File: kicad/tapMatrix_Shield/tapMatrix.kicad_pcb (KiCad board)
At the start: 2 copper layers, 68.6 x 53.3 mm, 29 parts, among them IC1 DS1307, P5 TS_ZIF, P6 LED_MATRIX_HDR, U1 APE8865N-33-HF-3, U2 MCP4921-E/SN, U3 74LS125, U4 TL072, U5 SD_CARD

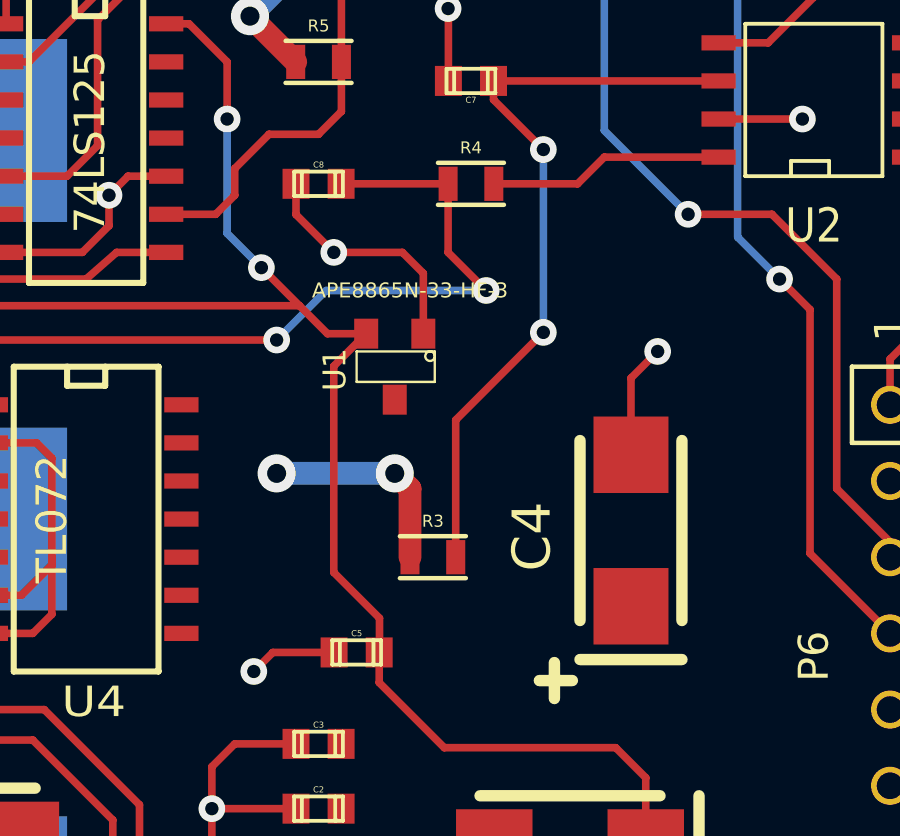
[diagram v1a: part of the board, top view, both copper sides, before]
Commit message: replace voltage regulator with corrected component
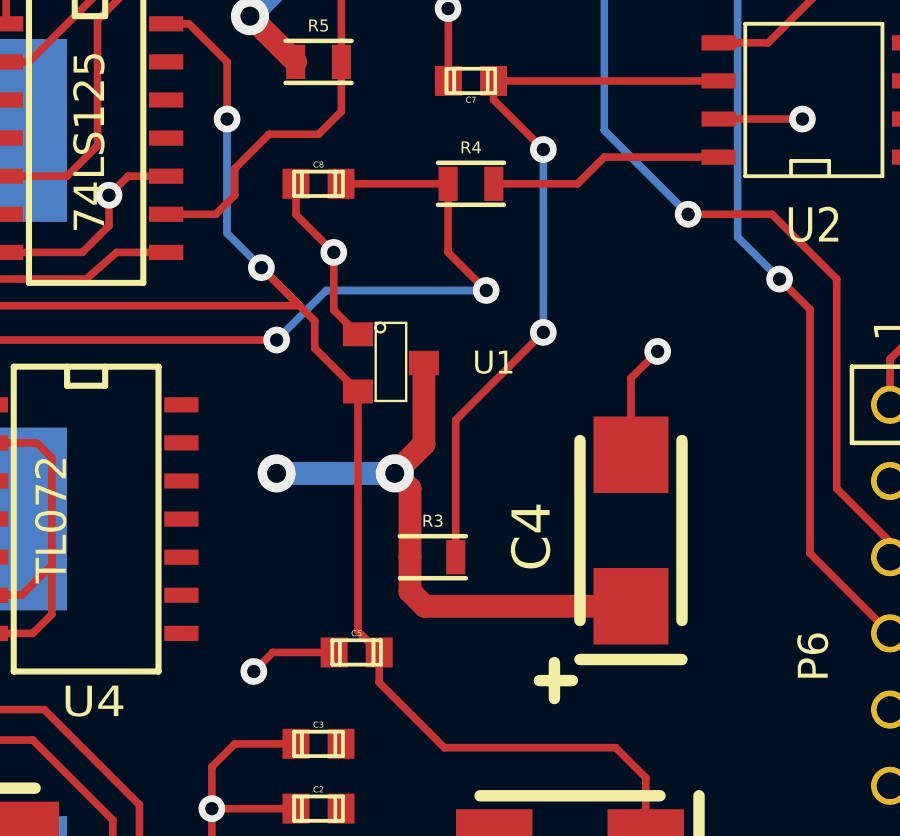
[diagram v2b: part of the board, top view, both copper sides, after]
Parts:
- U1: value APE8865N-33-HF-3 -> MCP1700T-3302E/MB
- moved U1 0.18 mm to (167.5, 106.6), turned to 270 degrees
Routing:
- net +5V: track 32.6 -> 45.4 mm
- net GND: track 94.1 -> 91.9 mm
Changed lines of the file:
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@@
     (thickness 1.6)
     (drawings 98)
-    (tracks 340)
+    (tracks 343)
     (zones 0)
     (modules 29)
@@
   (title_block
     (title "tapMatrix Shield: Footprint")
-    (date "24 Aug 2014")
-    (rev 0.1)
+    (date "03 Sep 2014")
+    (rev 0.2)
     (company "Responsive Devices Inc")
   )
@@
     )
   )
-  (module SMD_Packages:SOT-23 placed (layer F.Cu)
-    (at 167.64 106.68 180)
-    (tags SOT23)
-    (fp_text reference U1 (at 1.99898 -0.09906 270) (layer F.SilkS)
-      (effects (font (size 0.762 0.762) (thickness 0.11938)))
-    )
-    (fp_text value APE8865N-33-HF-3 (at -0.508 2.54 180) (layer F.SilkS)
-      (effects (font (size 0.50038 0.50038) (thickness 0.09906)))
-    )
-    (fp_circle (center -1.17602 0.35052) (end -1.30048 0.44958) (layer F.SilkS) (width 0.07874))
-    (fp_line (start 1.27 -0.508) (end 1.27 0.508) (layer F.SilkS) (width 0.07874))
-    (fp_line (start -1.3335 -0.508) (end -1.3335 0.508) (layer F.SilkS) (width 0.07874))
-    (fp_line (start 1.27 0.508) (end -1.3335 0.508) (layer F.SilkS) (width 0.07874))
-    (fp_line (start -1.3335 -0.508) (end 1.27 -0.508) (layer F.SilkS) (width 0.07874))
-    (pad 3 smd rect (at 0 -1.09982 180) (size 0.8001 1.00076) (layers F.Cu F.Paste F.Mask)
-      (net 1 +5V))
-    (pad 2 smd rect (at 0.9525 1.09982 180) (size 0.8001 1.00076) (layers F.Cu F.Paste F.Mask)
-      (net 49 +3.3V))
-    (pad 1 smd rect (at -0.9525 1.09982 180) (size 0.8001 1.00076) (layers F.Cu F.Paste F.Mask)
-      (net 2 GND))
-    (model smd\SOT23_3.wrl
-      (at (xyz 0 0 0))
-      (scale (xyz 0.4000000059604645 0.4000000059604645 0.4000000059604645))
-      (rotate (xyz 0 0 180))
-    )
-  )
   (module SMD_Packages:SOIC-8-N placed (layer F.Cu)
     (at 181.61 97.79 90)
@@
       (scale (xyz 1 1 1))
       (rotate (xyz 0 0 0))
+    )
+  )
+  (module SMD_Packages:SOT-23 (layer F.Cu)
+    (at 167.513 106.553 270)
+    (tags SOT23)
+    (fp_text reference U1 (at 0 -3.429 360) (layer F.SilkS)
+      (effects (font (size 0.762 0.762) (thickness 0.11938)))
+    )
+    (fp_text value MCP1700T-3302E/MB (at -1.905 -2.667 360) (layer F.SilkS) hide
+      (effects (font (size 0.50038 0.50038) (thickness 0.09906)))
+    )
+    (fp_circle (center -1.17602 0.35052) (end -1.30048 0.44958) (layer F.SilkS) (width 0.07874))
+    (fp_line (start 1.27 -0.508) (end 1.27 0.508) (layer F.SilkS) (width 0.07874))
+    (fp_line (start -1.3335 -0.508) (end -1.3335 0.508) (layer F.SilkS) (width 0.07874))
+    (fp_line (start 1.27 0.508) (end -1.3335 0.508) (layer F.SilkS) (width 0.07874))
+    (fp_line (start -1.3335 -0.508) (end 1.27 -0.508) (layer F.SilkS) (width 0.07874))
+    (pad 3 smd rect (at 0 -1.09982 270) (size 0.8001 1.00076) (layers F.Cu F.Paste F.Mask)
+      (net 1 +5V))
+    (pad 2 smd rect (at 0.9525 1.09982 270) (size 0.8001 1.00076) (layers F.Cu F.Paste F.Mask)
+      (net 49 +3.3V))
+    (pad 1 smd rect (at -0.9525 1.09982 270) (size 0.8001 1.00076) (layers F.Cu F.Paste F.Mask)
+      (net 2 GND))
+    (model smd\SOT23_3.wrl
+      (at (xyz 0 0 0))
+      (scale (xyz 0.4000000059604645 0.4000000059604645 0.4000000059604645))
+      (rotate (xyz 0 0 180))
     )
   )
@@
   (gr_line (start 0 0) (end 66.04 0) (layer Dwgs.User) (width 0.1))
   (gr_line (start 0 0) (end 0 -53.34) (layer Dwgs.User) (width 0.1))
+  (segment (start 168.148 113.03) (end 168.148 114.173) (width 0.762) (layer F.Cu) (net 1) (status 400000))
+  (segment (start 168.64076 114.66576) (end 175.514 114.66576) (width 0.762) (layer F.Cu) (net 1) (status 800000))
+  (segment (start 168.148 114.173) (end 168.64076 114.66576) (width 0.762) (layer F.Cu) (net 1))
+  (segment (start 168.61282 106.553) (end 168.61282 109.26318) (width 0.762) (layer F.Cu) (net 1) (status 400000))
+  (segment (start 168.61282 109.26318) (end 167.64 110.236) (width 0.762) (layer F.Cu) (net 1))
   (segment (start 184.785 99.695) (end 187.198 99.695) (width 0.762) (layer F.Cu) (net 1))
   (via (at 193.167 108.712) (size 1.27) (layers F.Cu B.Cu) (net 1))
@@
   (via (at 167.64 110.236) (size 1.27) (layers F.Cu B.Cu) (net 1))
   (segment (start 168.148 110.744) (end 167.64 110.236) (width 0.762) (layer F.Cu) (net 1))
+  (segment (start 165.608 102.87) (end 165.608 104.79532) (width 0.254) (layer F.Cu) (net 2))
+  (segment (start 164.34816 101.61016) (end 165.608 102.87) (width 0.254) (layer F.Cu) (net 2))
+  (via (at 165.608 102.87) (size 0.889) (layers F.Cu B.Cu) (net 2))
+  (segment (start 164.34816 100.584) (end 164.34816 101.61016) (width 0.254) (layer F.Cu) (net 2))
+  (segment (start 165.608 104.79532) (end 166.41318 105.6005) (width 0.254) (layer F.Cu) (net 2) (status 800000))
   (segment (start 178.435 98.425) (end 181.229 98.425) (width 0.254) (layer F.Cu) (net 2))
   (via (at 181.229 98.425) (size 0.889) (layers F.Cu B.Cu) (net 2))
@@
   (segment (start 140.843 88.138) (end 133.731 88.138) (width 0.254) (layer F.Cu) (net 2))
   (segment (start 142.085 89.38) (end 140.843 88.138) (width 0.254) (layer F.Cu) (net 2))
-  (segment (start 168.5925 105.58018) (end 168.5925 103.5685) (width 0.254) (layer F.Cu) (net 2))
-  (segment (start 164.34816 101.61016) (end 164.34816 100.584) (width 0.254) (layer F.Cu) (net 2))
-  (via (at 165.608 102.87) (size 0.889) (layers F.Cu B.Cu) (net 2))
-  (segment (start 164.34816 101.61016) (end 165.608 102.87) (width 0.254) (layer F.Cu) (net 2))
-  (segment (start 167.894 102.87) (end 165.608 102.87) (width 0.254) (layer F.Cu) (net 2))
-  (segment (start 168.5925 103.5685) (end 167.894 102.87) (width 0.254) (layer F.Cu) (net 2))
   (segment (start 169.672 113.03) (end 169.672 108.458) (width 0.254) (layer F.Cu) (net 3))
   (segment (start 170.93184 97.77984) (end 170.93184 97.155) (width 0.254) (layer F.Cu) (net 3))
@@
   (segment (start 144.526 101.6) (end 154.686 101.6) (width 0.254) (layer F.Cu) (net 48))
   (segment (start 139.256 96.33) (end 144.526 101.6) (width 0.254) (layer F.Cu) (net 48))
+  (segment (start 163.195 103.378) (end 164.973 105.156) (width 0.254) (layer F.Cu) (net 49))
+  (segment (start 164.973 106.06532) (end 166.41318 107.5055) (width 0.254) (layer F.Cu) (net 49) (status 800000))
+  (segment (start 164.973 105.156) (end 164.973 106.06532) (width 0.254) (layer F.Cu) (net 49))
+  (segment (start 166.41318 107.5055) (end 166.41318 115.49634) (width 0.254) (layer F.Cu) (net 49) (status 400000))
+  (segment (start 166.41318 115.49634) (end 167.12184 116.205) (width 0.254) (layer F.Cu) (net 49) (status 800000))
   (segment (start 167.12184 116.205) (end 167.12184 117.21084) (width 0.254) (layer F.Cu) (net 49))
   (segment (start 176.00676 120.38076) (end 176.00676 122.682) (width 0.254) (layer F.Cu) (net 49))
@@
   (segment (start 167.12184 117.21084) (end 169.291 119.38) (width 0.254) (layer F.Cu) (net 49))
   (segment (start 167.12184 116.205) (end 167.132 116.19484) (width 0.254) (layer F.Cu) (net 49))
-  (segment (start 167.132 116.19484) (end 167.132 115.062) (width 0.254) (layer F.Cu) (net 49))
-  (segment (start 167.132 115.062) (end 165.608 113.538) (width 0.254) (layer F.Cu) (net 49))
-  (segment (start 165.608 113.538) (end 165.608 106.65968) (width 0.254) (layer F.Cu) (net 49))
-  (segment (start 165.608 106.65968) (end 166.6875 105.58018) (width 0.254) (layer F.Cu) (net 49))
   (segment (start 136.12 95.23) (end 134.894 95.23) (width 0.254) (layer F.Cu) (net 49))
   (segment (start 135.89 104.648) (end 164.465 104.648) (width 0.254) (layer F.Cu) (net 49))
@@
   (segment (start 134.366 95.758) (end 134.366 103.124) (width 0.254) (layer F.Cu) (net 49))
   (segment (start 134.894 95.23) (end 134.366 95.758) (width 0.254) (layer F.Cu) (net 49))
-  (segment (start 166.6875 105.58018) (end 165.39718 105.58018) (width 0.254) (layer F.Cu) (net 49))
   (segment (start 160.782 95.25) (end 160.02 95.25) (width 0.254) (layer F.Cu) (net 49))
   (segment (start 162.052 96.52) (end 160.782 95.25) (width 0.254) (layer F.Cu) (net 49))
@@
   (segment (start 163.195 103.378) (end 162.052 102.235) (width 0.254) (layer B.Cu) (net 49))
   (via (at 163.195 103.378) (size 0.889) (layers F.Cu B.Cu) (net 49))
-  (segment (start 165.39718 105.58018) (end 164.465 104.648) (width 0.254) (layer F.Cu) (net 49))
   (segment (start 164.465 104.648) (end 163.195 103.378) (width 0.254) (layer F.Cu) (net 49))
   (zone (net 1) (net_name +5V) (layer F.Cu) (hatch edge 0.508)

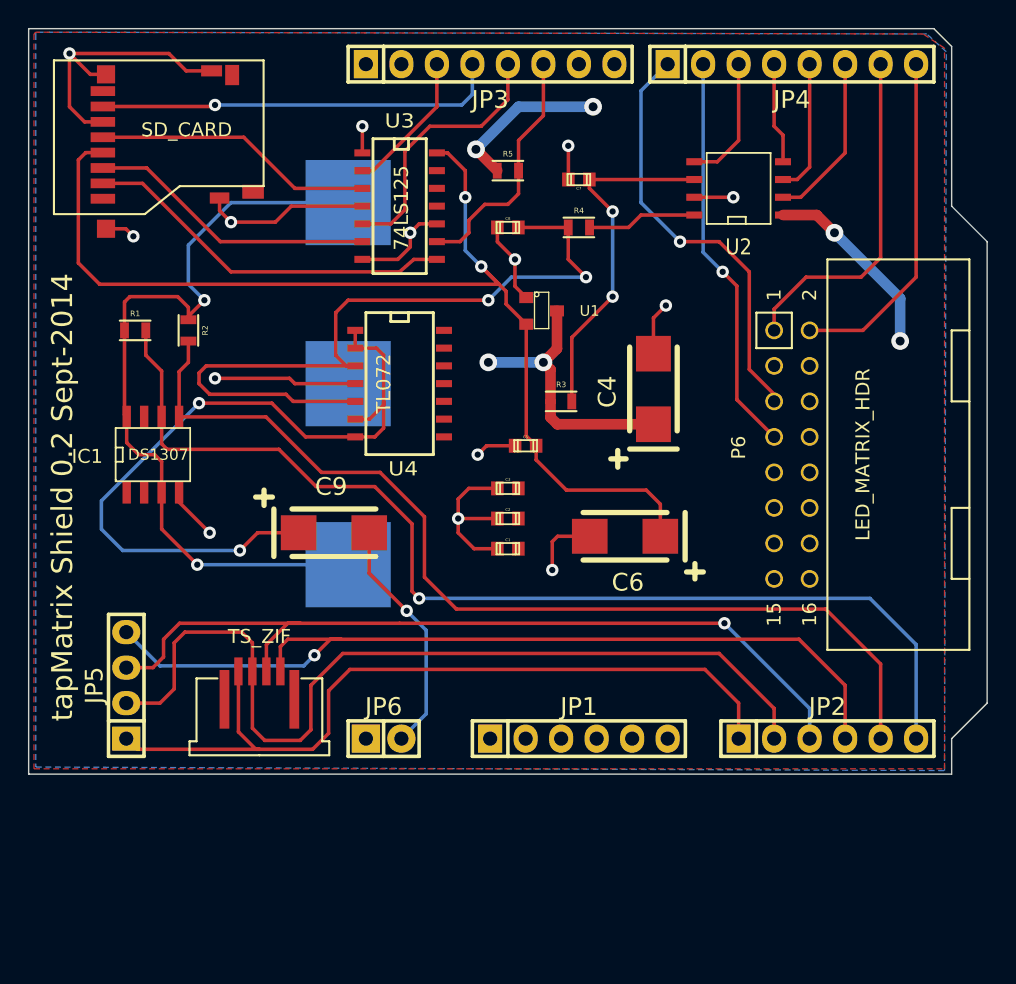
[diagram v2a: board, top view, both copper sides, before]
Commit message: create v0.3_ fix problems with U1, U3, U4 components U1 used the wrong footprint. changed from SOT-23 to SOT-89-3 U3 used the narrow version of SOIC-14 (incorrectly named in library as SOIC-14_W). changed to actual SOIC-14-Wide U4 incorrectly used SOIC-14 footprint. changed to SOIC-8 tore up the layout, placed new footprints. still need to reroute everything
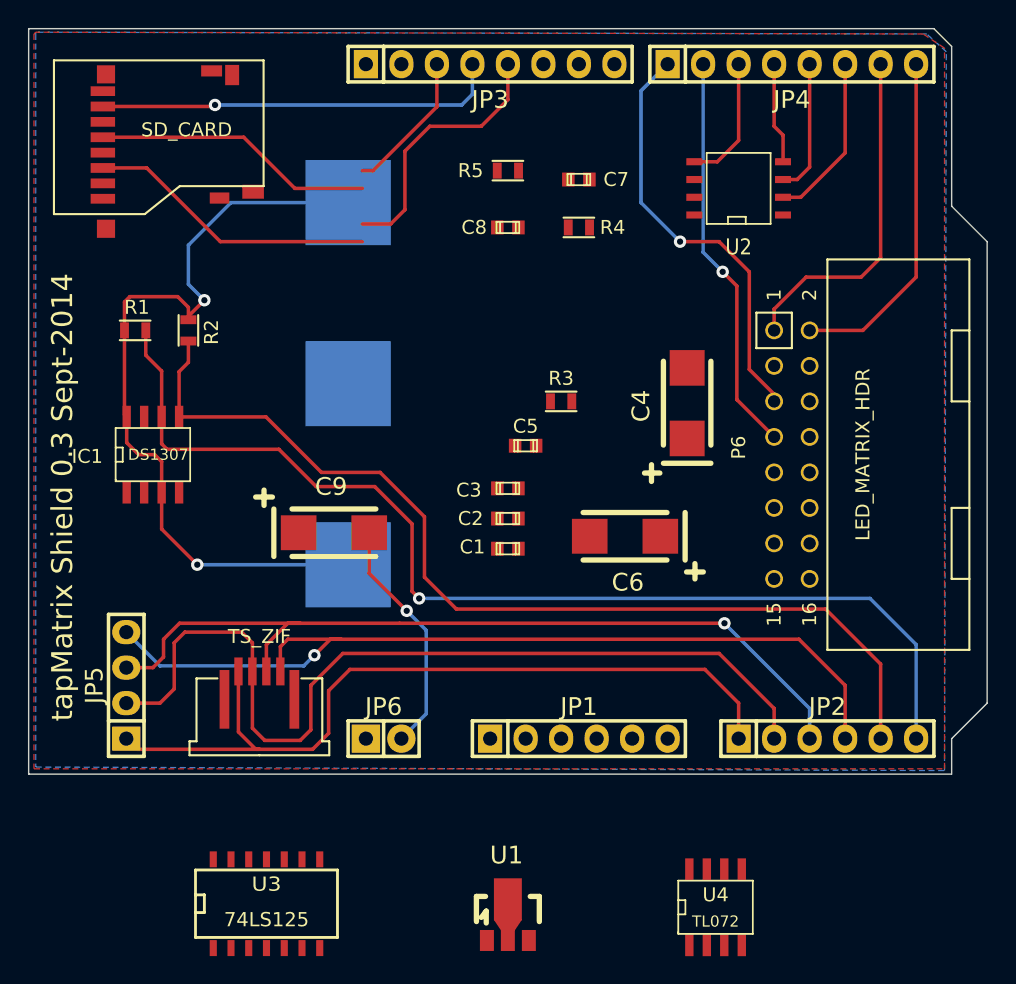
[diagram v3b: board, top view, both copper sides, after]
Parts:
- U1: footprint SMD_Packages:SOT-23 -> Housings_SOT-89:SOT89-3_Housing
- U3: footprint SMD_Packages:SOIC-14_W -> SMD_Packages:SOIC-14_N
- U4: footprint SMD_Packages:SOIC-14_N -> Housings_SOIC:SOIC-8_N
- moved U3 50.7 mm to (147.8, 148.8), turned to 0 degrees
- moved U4 43.7 mm to (180.0, 149.2), turned to 0 degrees
- moved U1 43.3 mm to (165.1, 149.8), turned to 0 degrees
- moved C4 2.62 mm to (177.9, 113.2)
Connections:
- C5 pad 1: +3.3V -> VCC
- C6 pad 1: +3.3V -> VCC
- U1 pad 2: +3.3V -> +5V
- U1 pad 3: +5V -> VCC
- U3 pad 14: +3.3V -> VCC
- U5 pad 4: +3.3V -> VCC
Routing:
- net GND: track 91.9 -> 0.00 mm, vias 14 -> 0
- net +3.3V: track 79.7 -> 0.00 mm, vias 2 -> 0
- net Net-(C8-Pad1): track 55.2 -> 0.00 mm, vias 2 -> 0
- net Net-(C9-Pad1): track 53.1 -> 0.00 mm, vias 2 -> 0
- net +5V: track 45.4 -> 0.00 mm, vias 6 -> 0
- net /CS: track 26.9 -> 0.00 mm
- net Net-(C7-Pad2): track 25.3 -> 0.00 mm, vias 2 -> 0
- net /SD_CS: track 17.8 -> 0.00 mm
- net Net-(R4-Pad2): track 7.86 -> 0.00 mm
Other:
- board text added: "tapMatrix Shield 0.3 Sept-2014"
- board text removed: "tapMatrix Shield 0.2 Sept-2014"

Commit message: Revised r0.3 components, tore up pcb
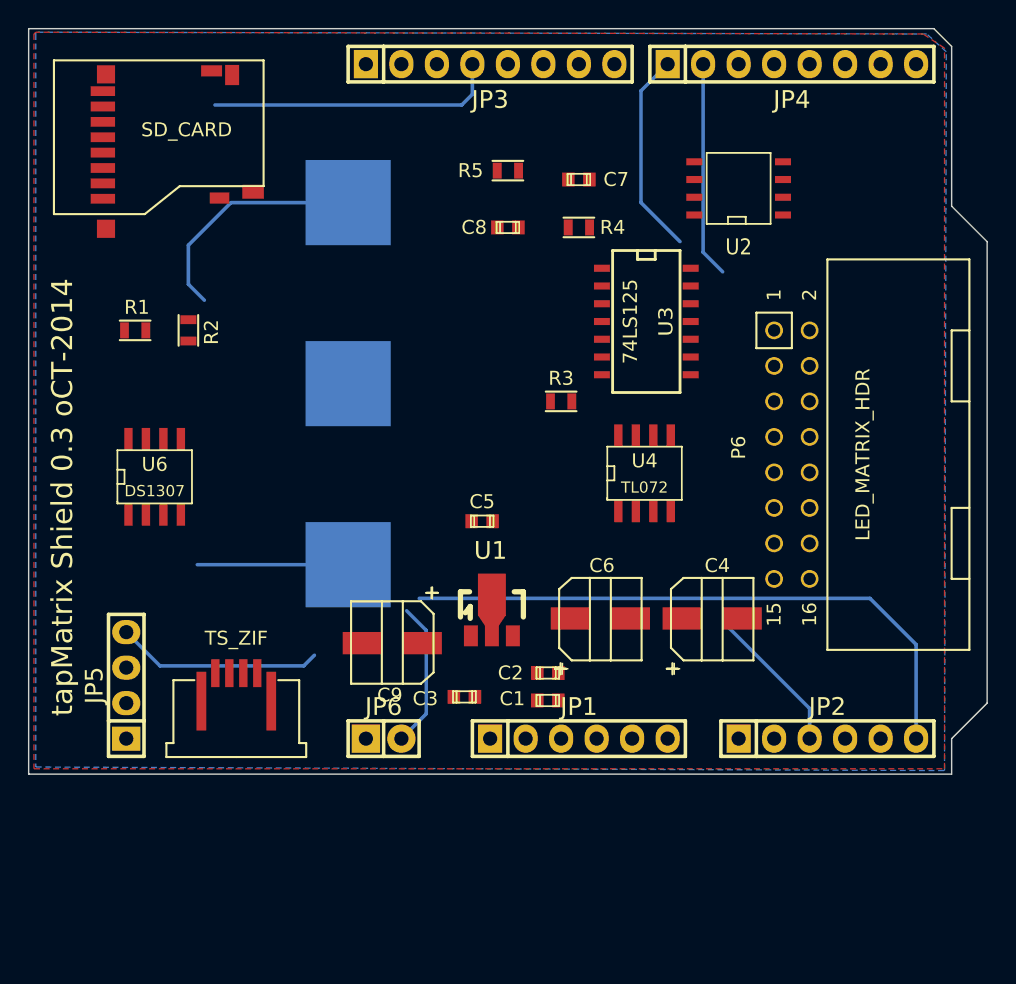
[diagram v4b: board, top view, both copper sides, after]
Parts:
- removed IC1: DS1307, Housings_SOIC:SOIC-8_N
- added U6: DS1307, tapmatrix:SOIC-8_N, F.Cu at (139.8, 118.4)
- C4, C6, C9: footprint Capacitors_Tantalum_SMD:TantalC_SizeC_EIA-6032_Reflow -> tapmatrix:EEE-0JA101WR
- moved U3 49.7 mm to (175.1, 107.3), turned to 270 degrees
- moved U4 31.5 mm to (174.9, 118.2)
- moved U1 21.8 mm to (164.0, 128.0)
- moved C4 15.4 mm to (179.8, 128.5), turned to 270 degrees
- moved C3 15.2 mm to (162.0, 134.2)
- moved C2 11.4 mm to (168.0, 132.5)
- moved C1 11.2 mm to (168.0, 134.4)
- moved C9 9.00 mm to (156.8, 130.4), turned to 90 degrees
- moved C5 6.23 mm to (163.3, 121.6)
- moved C6 6.03 mm to (171.8, 128.5), turned to 270 degrees
- moved P5 1.66 mm to (145.7, 133.5)
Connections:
- C5 pad 1: VCC -> +3.3V
- C6 pad 1: VCC -> +3.3V
- U1 pad 2: +5V -> +3.3V
- U1 pad 3: VCC -> +5V
- U3 pad 14: VCC -> +3.3V
- U5 pad 4: VCC -> +3.3V
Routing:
- net /I2C_SDA: track 71.1 -> 0.00 mm
- net /YP: track 65.4 -> 0.00 mm
- net /XM: track 58.2 -> 0.00 mm
- net /XP: track 61.6 -> 10.8 mm, vias 1 -> 0
- net /YM: track 64.7 -> 14.8 mm, vias 1 -> 0
- net /I2C_SCL: track 78.1 -> 43.7 mm, vias 1 -> 0
- net Net-(BT1-Pad1): track 58.6 -> 29.2 mm, vias 2 -> 0
- net /MATRIX_CS: track 24.5 -> 0.00 mm
- net /MATRIX_CLK: track 24.4 -> 0.00 mm
- net /DATA_IN: track 20.7 -> 0.00 mm
- net /SCLK: track 20.1 -> 0.00 mm
- net /MOSI: track 19.1 -> 0.00 mm
- net /MATRIX_WR: track 30.5 -> 14.6 mm, vias 1 -> 0
- net /MATRIX_DATA: track 28.8 -> 15.4 mm, vias 1 -> 0
- net /DAC_CS: track 12.1 -> 0.00 mm
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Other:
- board text added: "tapMatrix Shield 0.3 oCT-2014"
- board text removed: "tapMatrix Shield 0.3 Sept-2014"
